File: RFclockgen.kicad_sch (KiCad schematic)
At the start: 0 parts

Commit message: Clock Generator footprint and symbol
Added symbol, footprint, and model files for the ADF4351
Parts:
- added U1: ADF4351BCPZ-RL7, CP_32_7_ADI, symbol ADF4351BCPZ-RL7:ADF4351BCPZ-RL7
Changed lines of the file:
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@@
 	(generator_version "9.0")
 	(paper "A4")
+	(symbol
+		(lib_id "ADF4351BCPZ-RL7:ADF4351BCPZ-RL7")
+		(at 105.41 74.93 0)
+		(unit 1)
+		(exclude_from_sim no)
+		(in_bom yes)
+		(on_board yes)
+		(dnp no)
+		(fields_autoplaced yes)
+		(property "Reference" "U1"
+			(at 130.81 64.77 0)
+			(effects
+				(font
+					(size 1.524 1.524)
+				)
+			)
+		)
+		(property "Value" "ADF4351BCPZ-RL7"
+			(at 130.81 67.31 0)
+			(effects
+				(font
+					(size 1.524 1.524)
+				)
+			)
+		)
+		(property "Footprint" "CP_32_7_ADI"
+			(at 105.41 74.93 0)
+			(effects
+				(font
+					(size 1.27 1.27)
+					(italic yes)
+				)
+				(hide yes)
+			)
+		)
+		(property "Datasheet" "https://www.analog.com/media/en/technical-documentation/data-sheets/ADF4351.pdf"
+			(at 105.41 74.93 0)
+			(effects
+				(font
+					(size 1.27 1.27)
+					(italic yes)
+				)
+				(hide yes)
+			)
+		)
+		(property "Description" ""
+			(at 105.41 74.93 0)
+			(effects
+				(font
+					(size 1.27 1.27)
+				)
+				(hide yes)
+			)
+		)
+		(pin "32"
+		)
+		(pin "28"
+		)
+		(pin "9"
+		)
+		(pin "16"
+		)
+		(pin "12"
+		)
+		(pin "8"
+		)
+		(pin "31"
+		)
+		(pin "21"
+		)
+		(pin "19"
+		)
+		(pin "33"
+		)
+		(pin "11"
+		)
+		(pin "30"
+		)
+		(pin "3"
+		)
+		(pin "2"
+		)
+		(pin "4"
+		)
+		(pin "10"
+		)
+		(pin "14"
+		)
+		(pin "15"
+		)
+		(pin "7"
+		)
+		(pin "1"
+		)
+		(pin "6"
+		)
+		(pin "13"
+		)
+		(pin "5"
+		)
+		(pin "29"
+		)
+		(pin "26"
+		)
+		(pin "25"
+		)
+		(pin "24"
+		)
+		(pin "22"
+		)
+		(pin "27"
+		)
+		(pin "23"
+		)
+		(pin "20"
+		)
+		(pin "18"
+		)
+		(pin "17"
+		)
+		(instances
+			(project ""
+				(path "/e1444a2d-a0c4-493c-a136-c624dc084e46"
+					(reference "U1")
+					(unit 1)
+				)
+			)
+		)
+	)
 	(sheet_instances
 		(path "/"

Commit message: Added more components!
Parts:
- added L1: LQW15AN18NJ00D, LQW15AN18NJ00D:INDC1006X60N, symbol LQW15AN18NJ00D:LQW15AN18NJ00D
- added U2: ESP32-S3-WROOM-1, RF_Module:ESP32-S3-WROOM-1, symbol RF_Module:ESP32-S3-WROOM-1
- added U3: AP2112K-3.3, Package_TO_SOT_SMD:SOT-23-5, symbol Regulator_Linear:AP2112K-3.3
- added XTAL1: TSX-3225 24.0000MF20G-AC3, TSX-3225 24.0000MF20G-AC3_EPS, symbol TSX_3225_24_0000MF20G_AC3:TSX-3225_24.0000MF20G-AC3
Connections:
- new net: U2.1 (GND), U2.40 (GND), U2.41 (GND)

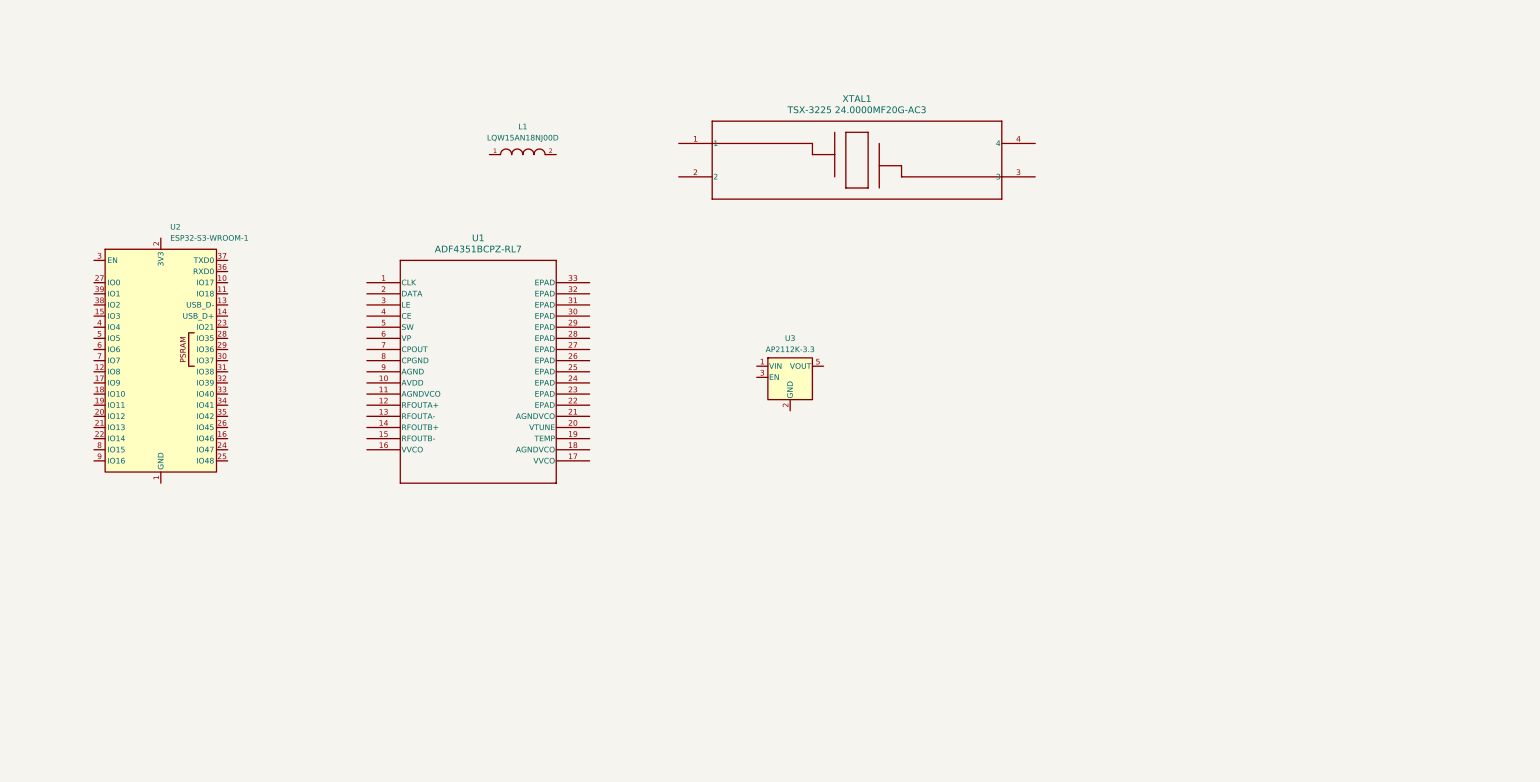
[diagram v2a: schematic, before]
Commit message: Finished Schematic
Finished schematic with all footprints based off of the hand drawn schematic
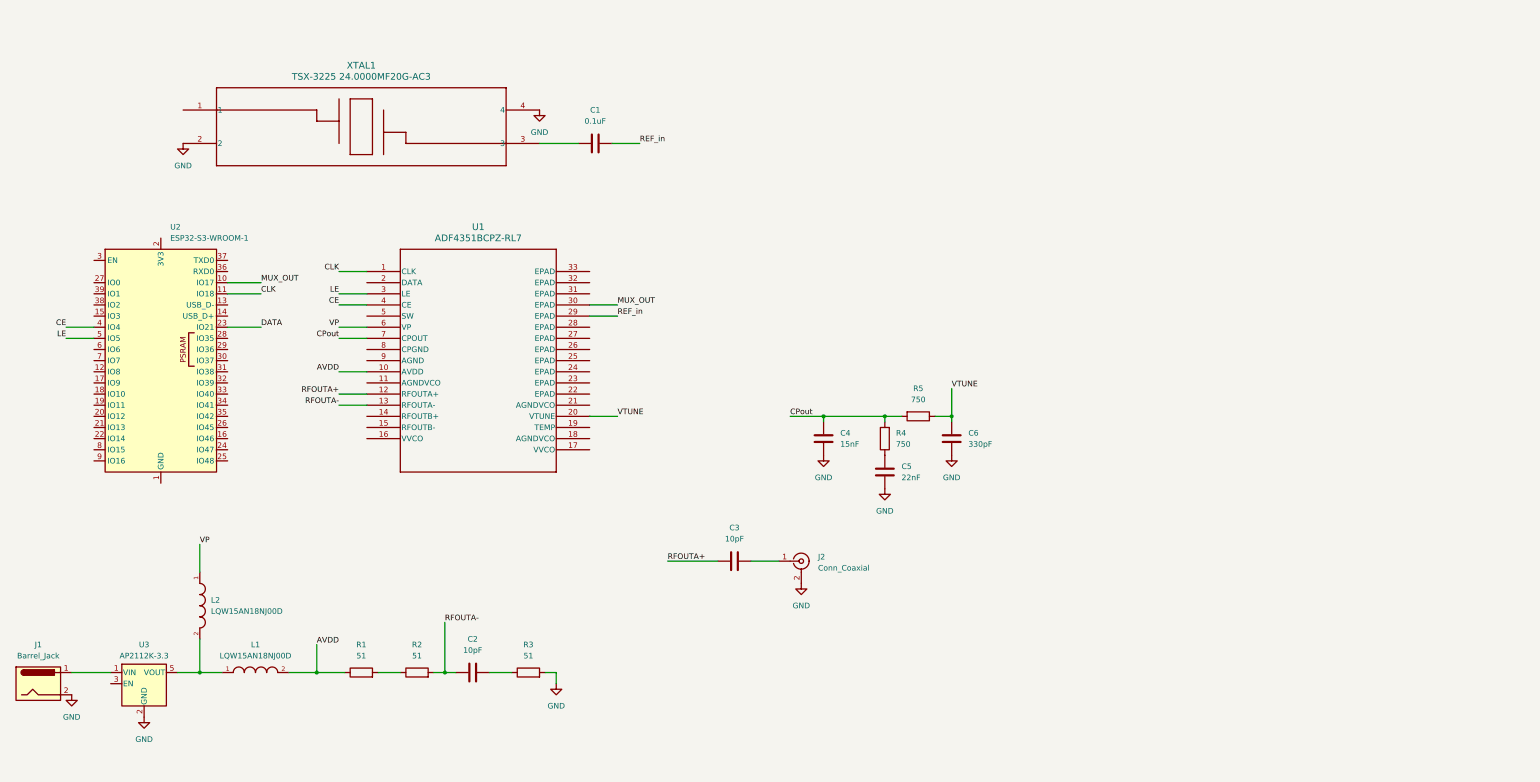
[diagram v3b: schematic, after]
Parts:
- added C1: 0.1uF, Capacitor_SMD:C_0603_1608Metric_Pad1.08x0.95mm_HandSolder, symbol Device:C
- added C2, C3: 10pF, Capacitor_SMD:C_0603_1608Metric_Pad1.08x0.95mm_HandSolder, symbol Device:C
- added C4: 15nF, Capacitor_SMD:C_0603_1608Metric_Pad1.08x0.95mm_HandSolder, symbol Device:C
- added C5: 22nF, Capacitor_SMD:C_0603_1608Metric_Pad1.08x0.95mm_HandSolder, symbol Device:C
- added C6: 330pF, Capacitor_SMD:C_0603_1608Metric_Pad1.08x0.95mm_HandSolder, symbol Device:C
- added J1: Barrel_Jack, Connector_BarrelJack:BarrelJack_CUI_PJ-063AH_Horizontal, symbol Connector:Barrel_Jack
- added J2: Conn_Coaxial, Connector_Coaxial:SMA_Samtec_SMA-J-P-H-ST-EM1_EdgeMount, symbol Connector:Conn_Coaxial
- added L2: LQW15AN18NJ00D, LQW15AN18NJ00D:INDC1006X60N, symbol LQW15AN18NJ00D:LQW15AN18NJ00D
- added R1, R2, R3: 51, Resistor_SMD:R_0603_1608Metric_Pad0.98x0.95mm_HandSolder, symbol Device:R
- added R4, R5: 750, Resistor_SMD:R_0603_1608Metric_Pad0.98x0.95mm_HandSolder, symbol Device:R
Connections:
- net GND: now reaches XTAL1.2
- net GND: now also U3.2 (GND), XTAL1.4, C4.2, C5.2, C6.2, J1.2, J2.2 (Ext), R3.2
- net at XTAL1.3: now also C1.2
- net at U3.1 (VIN): now also J1.1
- net at U3.5 (VOUT): now also L1.1, L2.2
- net AVDD: now reaches L1.2
- net AVDD: now also U1.10 (AVDD), R1.1
- net MUX_OUT: now reaches U2.10 (IO17)
- net MUX_OUT: now also U1.30 (EPAD)
- net CLK: now reaches U2.11 (IO18)
- net CLK: now also U1.1 (CLK)
- net DATA: now reaches U2.23 (IO21)
- net CE: now reaches U2.4 (IO4)
- net CE: now also U1.4 (CE)
- net LE: now reaches U2.5 (IO5)
- net LE: now also U1.3 (LE)
- net RFOUTA+: now reaches U1.12 (RFOUTA+)
- net RFOUTA+: now also C3.2
- net RFOUTA-: now reaches U1.13 (RFOUTA-)
- net RFOUTA-: now also C2.2, R2.2
- net VTUNE: now reaches U1.20 (VTUNE)
- net VTUNE: now also C6.1, R5.1
- net REF_in: now reaches U1.29 (EPAD)
- net REF_in: now also C1.1
- net VP: now reaches U1.6 (VP)
- net VP: now also L2.1
- net CPout: now reaches U1.7 (CPOUT)
- net CPout: now also C4.1, R4.2, R5.2
- new net: C5.1, R4.1
- new net: C3.1, J2.1 (In)
- new net: R1.2, R2.1
- new net: C2.1, R3.1
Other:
- moved on the sheet: L1, U1, U3, XTAL1

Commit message: Changed clock IC
Changed clock IC symbol
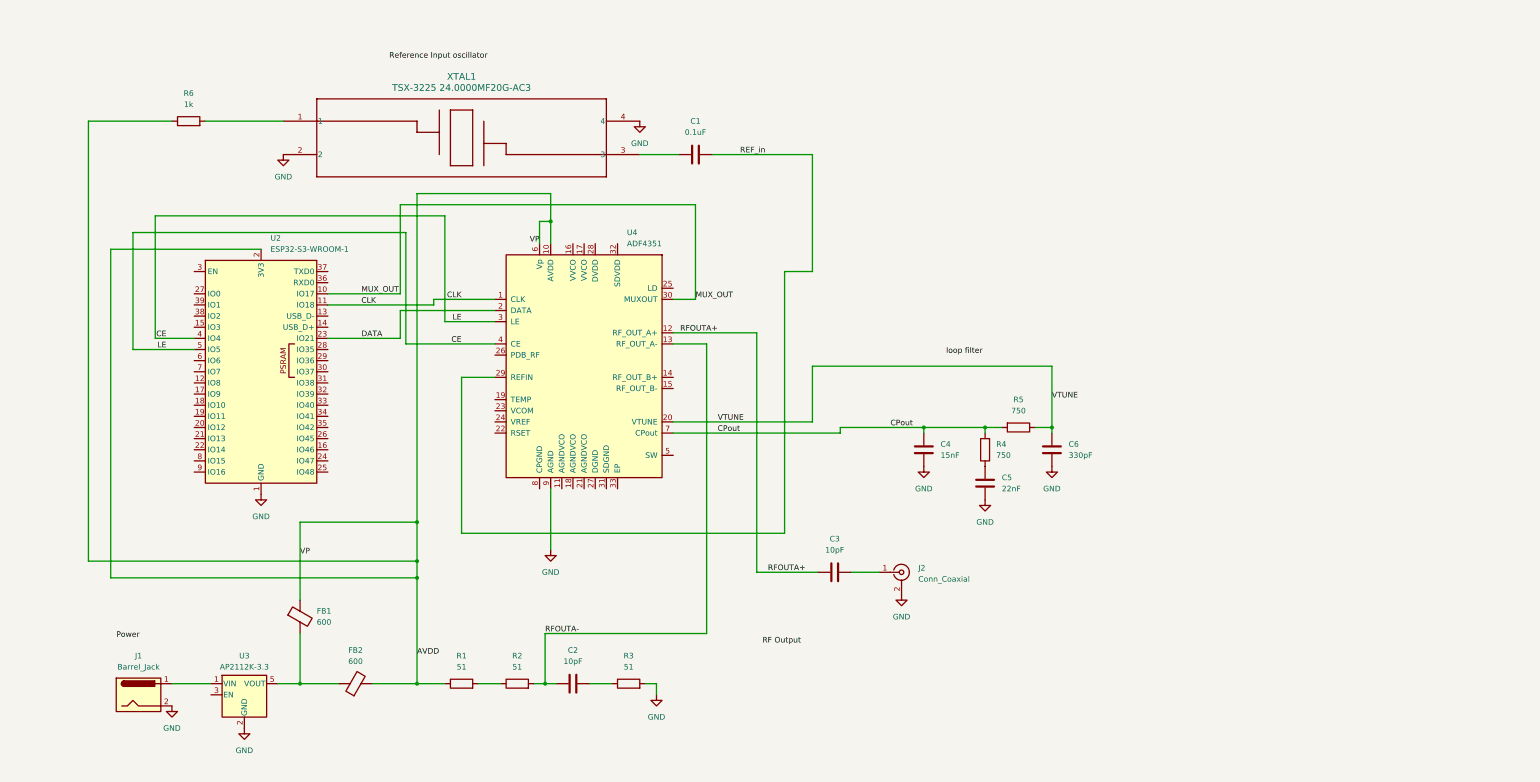
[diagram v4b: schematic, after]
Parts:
- removed L1, L2: LQW15AN18NJ00D, LQW15AN18NJ00D:INDC1006X60N, symbol LQW15AN18NJ00D:LQW15AN18NJ00D
- removed U1: ADF4351BCPZ-RL7, CP_32_7_ADI, symbol ADF4351BCPZ-RL7:ADF4351BCPZ-RL7
- added FB1, FB2: 600, symbol Device:FerriteBead
- added R6: 1k, symbol Device:R
- added U4: ADF4351, Package_CSP:LFCSP-32-1EP_5x5mm_P0.5mm_EP3.25x3.25mm, symbol Timer_PLL:ADF4351
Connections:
- net LE is gone; now on net CE: U2.5 (IO5)
- net AVDD: now also U2.2 (3V3), FB1.1, FB2.2, R6.1, U4.10 (AVDD), U4.6 (Vp)
- net CE: now also U4.3 (LE), U4.4 (CE)
- net CLK: now also U4.1 (CLK)
- net CPout: now also U4.7 (CPout)
- net DATA: now also U4.2 (DATA)
- net GND: now also U2.1 (GND), U2.40 (GND), U2.41 (GND), U4.9 (AGND)
- net MUX_OUT: now also U4.30 (MUXOUT)
- net REF_in: now also U4.29 (REFIN)
- net RFOUTA+: now also U4.12 (RF_OUT_A+)
- net RFOUTA-: now also U4.13 (RF_OUT_A-)
- net VTUNE: now also U4.20 (VTUNE)
- net at XTAL1.1: now also R6.2
- net at U3.5 (VOUT): now also FB1.2, FB2.1
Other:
- moved on the sheet: C1, C2, C3, C4, C5, C6, J1, J2, R1, R2, R3, R4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

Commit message: Fix: Added Global Labels
Cleaned up messy and overlapping wires by adding global labels
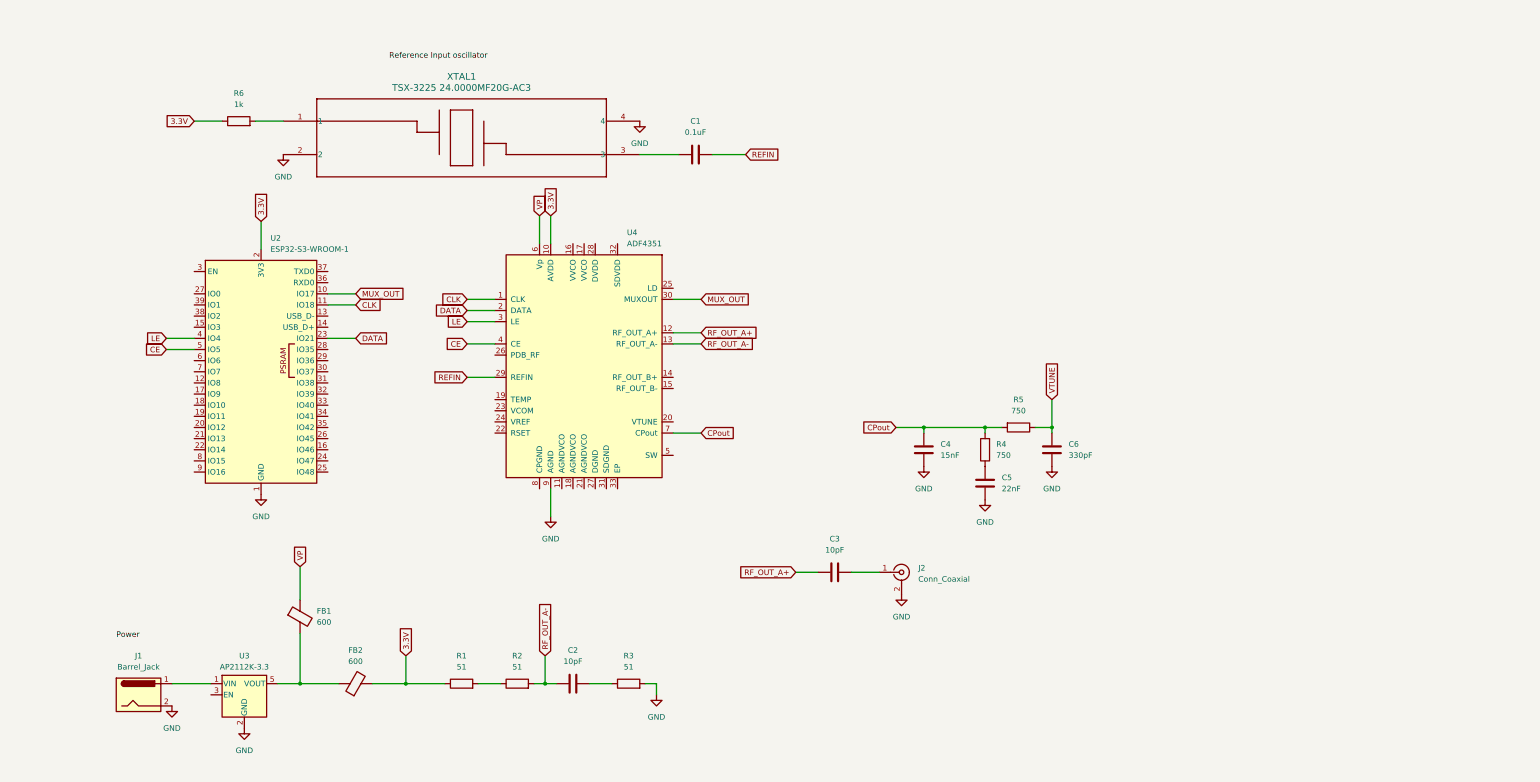
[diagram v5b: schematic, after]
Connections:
- net CE: no longer U2.4 (IO4), U4.3 (LE)
- net VTUNE: no longer U4.20 (VTUNE)
- net AVDD renamed 3.3V
- net 3.3V: no longer FB1.1, U4.6 (Vp)
- net REF_in renamed REFIN
- net RFOUTA+ renamed RF_OUT_A+
- net RFOUTA- renamed RF_OUT_A-
- new net LE: U2.4 (IO4), U4.3 (LE)
- new net VP: FB1.1, U4.6 (Vp)
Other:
- moved on the sheet: R6

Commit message: Created different schematic pages
Made multiple schematic pages for different components for easy viewing and access
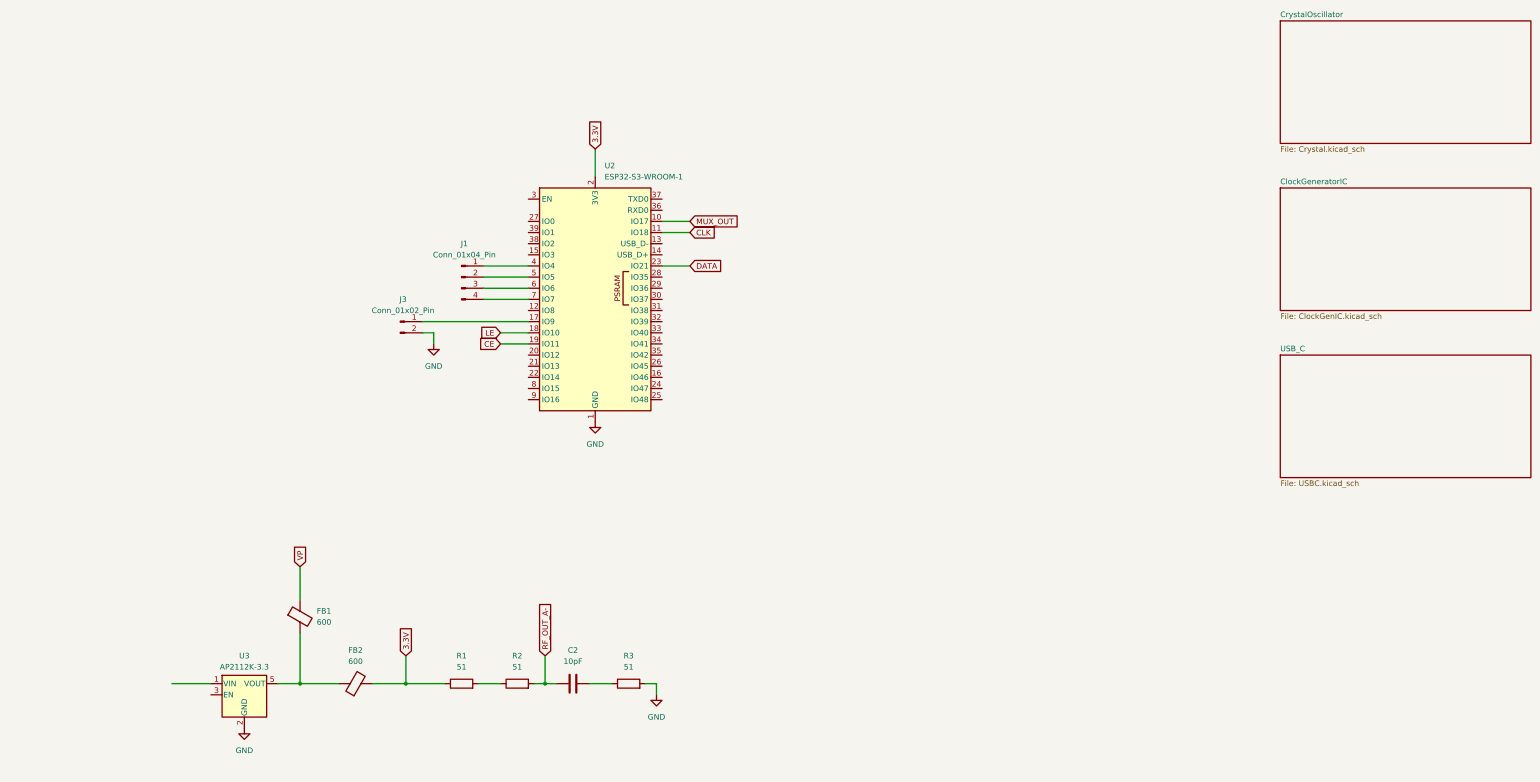
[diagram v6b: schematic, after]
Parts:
- removed C1: 0.1uF, Capacitor_SMD:C_0603_1608Metric_Pad1.08x0.95mm_HandSolder, symbol Device:C
- removed C3: 10pF, Capacitor_SMD:C_0603_1608Metric_Pad1.08x0.95mm_HandSolder, symbol Device:C
- removed C4: 15nF, Capacitor_SMD:C_0603_1608Metric_Pad1.08x0.95mm_HandSolder, symbol Device:C
- removed C5: 22nF, Capacitor_SMD:C_0603_1608Metric_Pad1.08x0.95mm_HandSolder, symbol Device:C
- removed C6: 330pF, Capacitor_SMD:C_0603_1608Metric_Pad1.08x0.95mm_HandSolder, symbol Device:C
- removed J1: Barrel_Jack, Connector_BarrelJack:BarrelJack_CUI_PJ-063AH_Horizontal, symbol Connector:Barrel_Jack
- removed J2: Conn_Coaxial, Connector_Coaxial:SMA_Samtec_SMA-J-P-H-ST-EM1_EdgeMount, symbol Connector:Conn_Coaxial
- removed R4, R5: 750, Resistor_SMD:R_0603_1608Metric_Pad0.98x0.95mm_HandSolder, symbol Device:R
- removed R6: 1k, symbol Device:R
- removed U4: ADF4351, Package_CSP:LFCSP-32-1EP_5x5mm_P0.5mm_EP3.25x3.25mm, symbol Timer_PLL:ADF4351
- removed XTAL1: TSX-3225 24.0000MF20G-AC3, TSX-3225 24.0000MF20G-AC3_EPS, symbol TSX_3225_24_0000MF20G_AC3:TSX-3225_24.0000MF20G-AC3
- added J1: Conn_01x04_Pin, symbol Connector:Conn_01x04_Pin
- added J3: Conn_01x02_Pin, symbol Connector:Conn_01x02_Pin
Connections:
- net CE: now also U2.19 (IO11); no longer U2.5 (IO5)
- net GND: now also J3.2 (Pin_2)
- net LE: now also U2.18 (IO10); no longer U2.4 (IO4)
- net at U2.17 (IO9): now also J3.1 (Pin_1)
- net at U2.6 (IO6): now also J1.3 (Pin_3)
- net at U2.7 (IO7): now also J1.4 (Pin_4)
- new net: J1.1 (Pin_1), U2.4 (IO4)
- new net: J1.2 (Pin_2), U2.5 (IO5)
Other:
- added sheet ClockGeneratorIC (ClockGenIC.kicad_sch)
- added sheet CrystalOscillator (Crystal.kicad_sch)
- added sheet USB_C (USBC.kicad_sch)
- moved on the sheet: U2
